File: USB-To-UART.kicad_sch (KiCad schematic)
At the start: 11 parts, among them U2 UMH3N, U4 CH340X

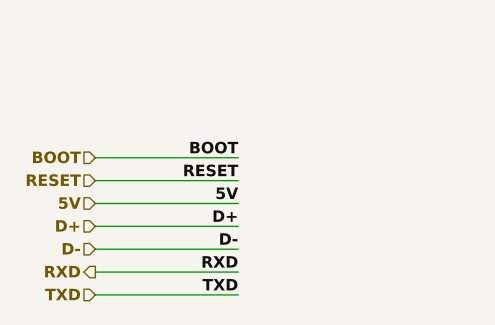
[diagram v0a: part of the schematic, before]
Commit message: Corrected RS485 schematic
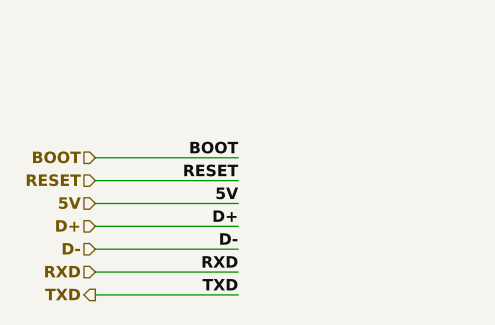
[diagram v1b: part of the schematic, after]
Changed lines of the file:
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@@
     (effects (font (size 1.27 1.27) (thickness 0.254) bold (color 255 0 0 1)) (justify right))
   )
-  (hierarchical_label "TXD" (shape input) (at 31.115 175.895 180) (fields_autoplaced)
+  (hierarchical_label "TXD" (shape output) (at 31.115 175.895 180) (fields_autoplaced)
     (effects (font (size 1.27 1.27) (thickness 0.254) bold (color 0 0 255 1)) (justify right))
   )
@@
     (effects (font (size 1.27 1.27) bold (color 0 194 0 1)) (justify right))
   )
-  (hierarchical_label "RXD" (shape output) (at 31.115 173.355 180) (fields_autoplaced)
+  (hierarchical_label "RXD" (shape input) (at 31.115 173.355 180) (fields_autoplaced)
     (effects (font (size 1.27 1.27) (thickness 0.254) bold (color 0 0 255 1)) (justify right))
   )

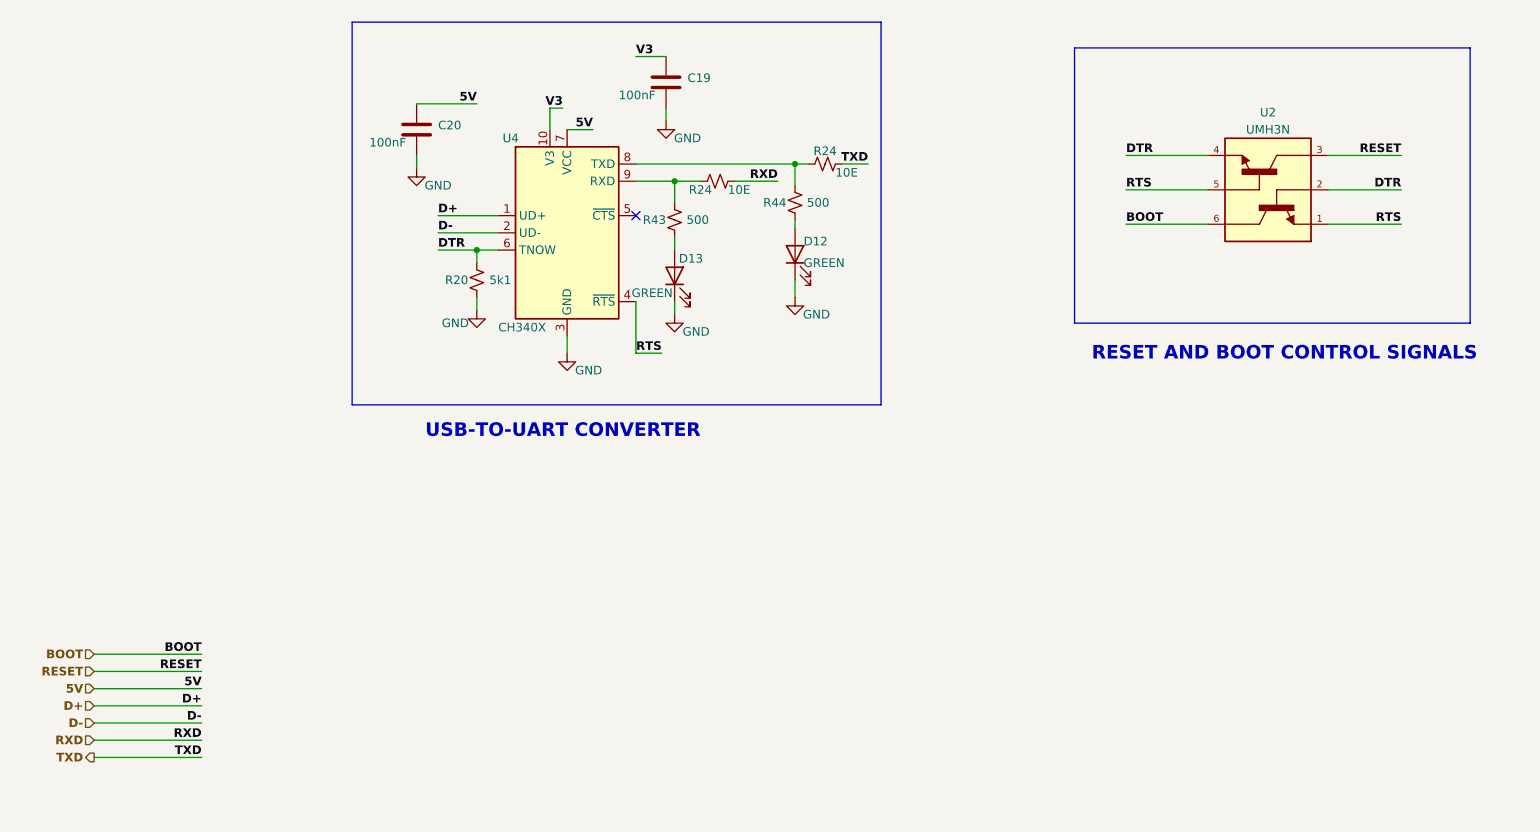
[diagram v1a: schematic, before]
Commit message: Arranged IP5306, Added support for USB-To-RS485
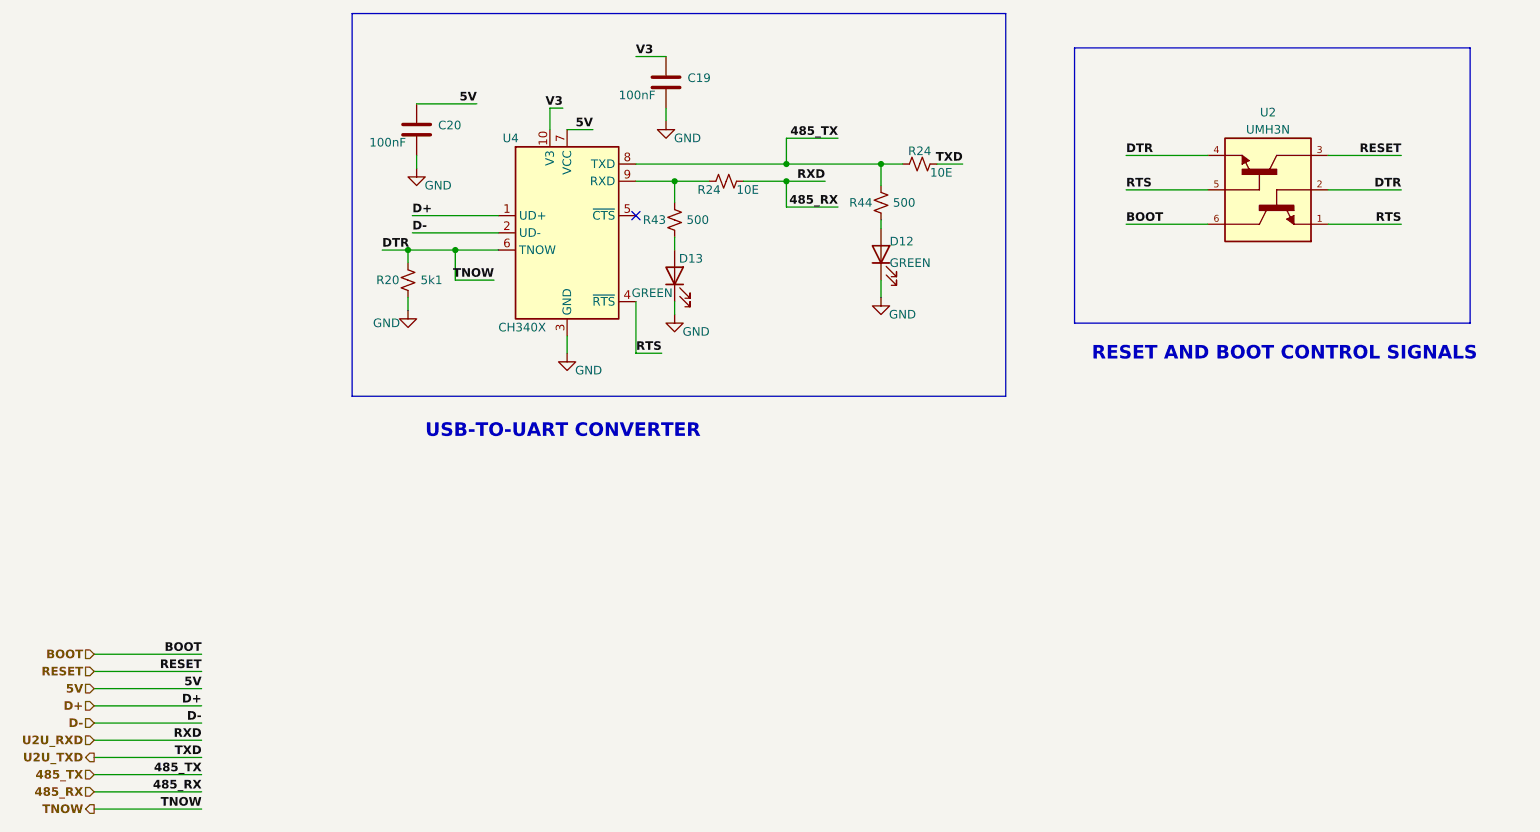
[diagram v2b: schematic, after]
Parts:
- U2: footprint UMH3N:UMT6 -> ESP32-S3_Dev_Board:SC-70-6_L2.2-W1.3-P0.65-LS2.1-BR; Availability In Stock -> (none); Check_prices https://www.snapeda.com/parts/UMH3N/Rohm/view-part/?ref=eda -> (none); MF Rohm -> (none); MP UMH3N -> (none); PN (none) -> UMH3N; Package SOT-363 Rohm -> (none); Price None -> (none); SnapEDA_Link https://www.snapeda.com/parts/UMH3N/Rohm/view-part/?ref=snap -> (none)
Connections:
- net 485_TX: now reaches R24.1, R44.2, U4.8 (TXD)
- net DTR renamed TNOW
- net RXD renamed 485_RX
- net TXD renamed U2U_TXD
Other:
- moved on the sheet: D12, R20, R24, R44

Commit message: Added selection jumper sheet and USB-UART option for board
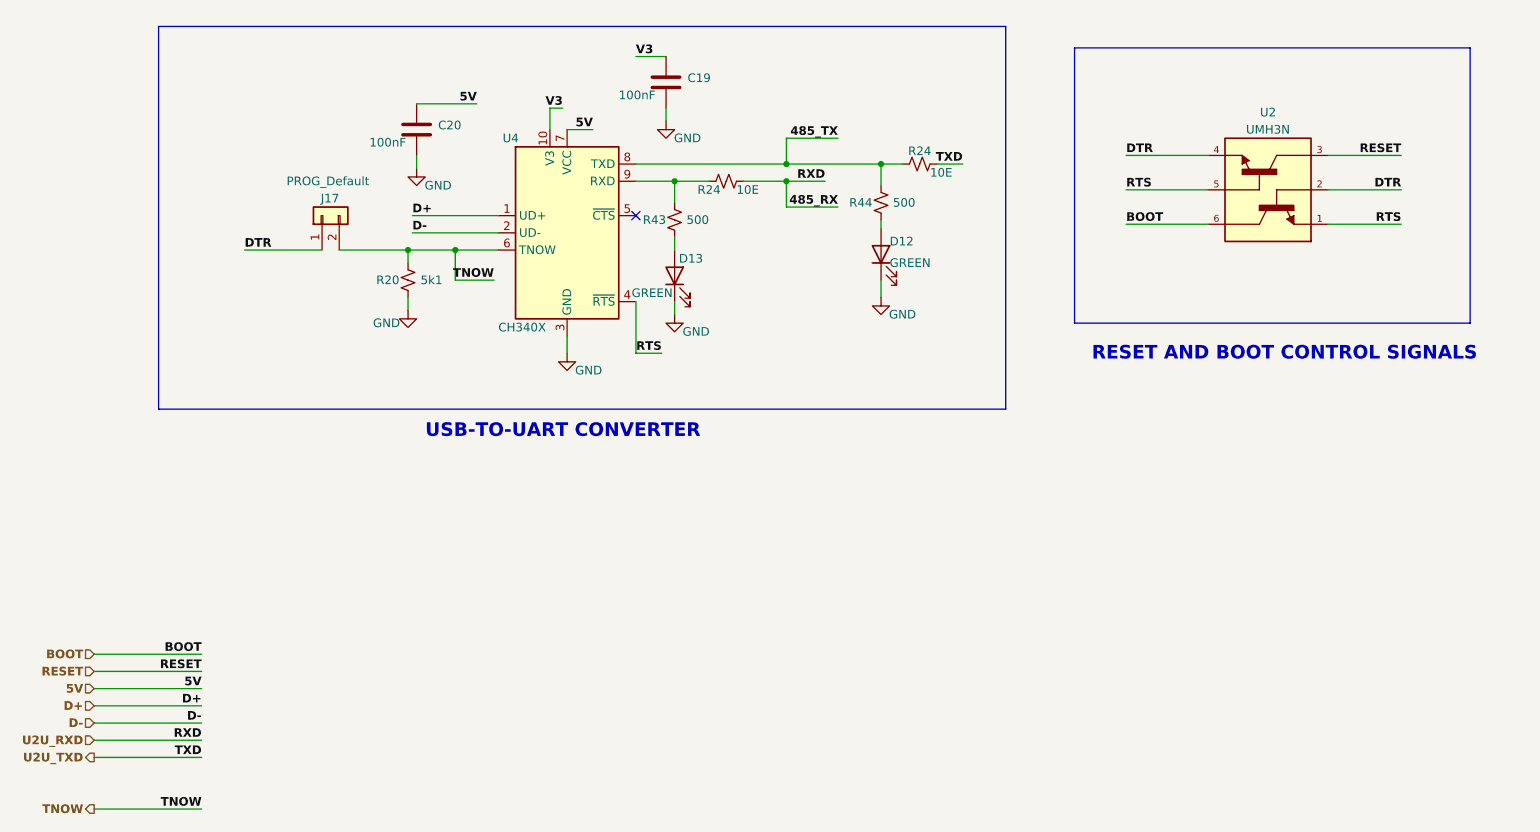
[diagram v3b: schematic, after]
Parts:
- added J17: PROG_Default, ESP32-S3_Dev_Board:PinHeader_1x02_P1.27mm_Vertical, symbol ESP32-S3_DB:Conn_01x02
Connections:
- net TNOW: now also J17.2 (Pin_2); no longer U2.2, U2.4
- net 485_RX renamed U2U_RXD
- new net DTR: J17.1 (Pin_1), U2.2, U2.4
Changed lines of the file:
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@@
   (junction (at 147.32 88.265) (diameter 0) (color 0 0 0 0)
   )
+  (junction (at 133.35 88.265) (diameter 0) (color 0 0 0 0)
+  )
+  (junction (at 116.84 90.805) (diameter 0) (color 0 0 0 0)
+  )
   (junction (at 77.47 100.965) (diameter 0) (color 0 0 0 0)
-  )
-  (junction (at 133.35 88.265) (diameter 0) (color 0 0 0 0)
-  )
-  (junction (at 116.84 90.805) (diameter 0) (color 0 0 0 0)
   )
   (junction (at 84.455 100.965) (diameter 0) (color 0 0 0 0)
@@
     (stroke (width 0) (type default))
   )
+  (wire (pts (xy 77.47 100.965) (xy 77.47 102.87))
+    (stroke (width 0) (type default))
+  )
   (wire (pts (xy 116.84 100.965) (xy 116.84 99.06))
     (stroke (width 0) (type default))
@@
     (stroke (width 0) (type default))
   )
+  (wire (pts (xy 67.31 100.965) (xy 77.47 100.965))
+    (stroke (width 0) (type default))
+  )
   (wire (pts (xy 183.515 97.155) (xy 195.58 97.155))
     (stroke (width 0) (type default))
@@
     (stroke (width 0) (type default))
   )
-  (wire (pts (xy 46.99 178.435) (xy 31.115 178.435))
-    (stroke (width 0.5) (type default) (color 0 0 255 1))
-  )
-  (wire (pts (xy 73.66 100.965) (xy 77.47 100.965))
-    (stroke (width 0) (type default))
-  )
-  (wire (pts (xy 77.47 100.965) (xy 77.47 102.87))
+  (wire (pts (xy 53.34 100.965) (xy 64.77 100.965))
     (stroke (width 0) (type default))
   )
@@
     (stroke (width 0.5) (type default) (color 128 77 0 1))
   )
-  (wire (pts (xy 46.99 180.975) (xy 31.115 180.975))
-    (stroke (width 0.5) (type default) (color 0 0 255 1))
-  )
   (wire (pts (xy 84.455 105.41) (xy 84.455 100.965))
     (stroke (width 0) (type default))
@@
     (stroke (width 1) (type default) (color 72 72 72 1))
   )
-  (bus (pts (xy 165.735 66.04) (xy 165.735 122.555))
+  (bus (pts (xy 165.735 67.945) (xy 165.735 124.46))
     (stroke (width 1) (type default) (color 72 72 72 1))
   )
@@
     (stroke (width 0.5) (type default) (color 0 0 255 1))
   )
-  (bus (pts (xy 69.215 66.04) (xy 165.735 66.04))
+  (bus (pts (xy 40.64 67.945) (xy 165.735 67.945))
     (stroke (width 1) (type default) (color 72 72 72 1))
   )
@@
     (stroke (width 1) (type default) (color 72 72 72 1))
   )
-  (bus (pts (xy 165.735 122.555) (xy 69.215 122.555))
+  (bus (pts (xy 165.735 124.46) (xy 40.64 124.46))
     (stroke (width 1) (type default) (color 72 72 72 1))
   )
@@
     (stroke (width 0) (type default))
   )
-  (bus (pts (xy 69.215 66.04) (xy 69.215 122.555))
+  (bus (pts (xy 40.64 67.945) (xy 40.64 124.46))
     (stroke (width 1) (type default) (color 72 72 72 1))
   )
@@
     (effects (font (size 1.27 1.27) bold (color 132 0 0 1)) (justify right bottom))
   )
-  (label "DTR" (at 73.66 100.965 0) (fields_autoplaced)
+  (label "DTR" (at 53.34 100.965 0) (fields_autoplaced)
     (effects (font (size 1.27 1.27) bold (color 221 133 0 1)) (justify left bottom))
   )
@@
     (effects (font (size 1.27 1.27) bold (color 0 194 0 1)) (justify right bottom))
   )
-  (label "485_TX" (at 46.99 178.435 180) (fields_autoplaced)
-    (effects (font (size 1.27 1.27) bold (color 0 0 255 1)) (justify right bottom))
-  )
   (label "D-" (at 46.99 170.815 180) (fields_autoplaced)
     (effects (font (size 1.27 1.27) bold (color 0 0 255 1)) (justify right bottom))
@@
     (effects (font (size 1.27 1.27) bold (color 0 0 255 1)) (justify right bottom))
   )
-  (label "485_RX" (at 46.99 180.975 180) (fields_autoplaced)
-    (effects (font (size 1.27 1.27) bold (color 0 0 255 1)) (justify right bottom))
-  )
   (label "RTS" (at 224.155 97.155 180) (fields_autoplaced)
     (effects (font (size 1.27 1.27) bold (color 221 133 0 1)) (justify right bottom))
@@
   (label "DTR" (at 183.515 86.995 0) (fields_autoplaced)
     (effects (font (size 1.27 1.27) bold (color 221 133 0 1)) (justify left bottom))
-  )
-  (hierarchical_label "485_RX" (shape input) (at 31.115 180.975 180) (fields_autoplaced)
-    (effects (font (size 1.27 1.27) (thickness 0.254) bold (color 0 0 255 1)) (justify right))
-  )
-  (hierarchical_label "485_TX" (shape input) (at 31.115 178.435 180) (fields_autoplaced)
-    (effects (font (size 1.27 1.27) (thickness 0.254) bold (color 0 0 255 1)) (justify right))
   )
   (hierarchical_label "D-" (shape input) (at 31.115 170.815 180) (fields_autoplaced)
@@
         )
       )
+    )
+  )
+  (symbol (lib_id "ESP32-S3_DB:Conn_01x02") (at 64.77 95.885 90) (unit 1)
+    (in_bom yes) (on_board yes) (dnp no)
+    (property "Reference" "J17" (at 67.31 93.345 90)
+      (effects (font (size 1.27 1.27)) (justify left))
+    )
+    (property "Value" "PROG_Default" (at 71.755 90.805 90)
+      (effects (font (size 1.27 1.27)) (justify left))
+    )
+    (property "Footprint" "ESP32-S3_Dev_Board:PinHeader_1x02_P1.27mm_Vertical" (at 64.77 95.885 0)
+      (effects (font (size 1.27 1.27)) hide)
+    )
+    (property "Datasheet" "~" (at 64.77 95.885 0)
+      (effects (font (size 1.27 1.27)) hide)
+    )
+    (property "PN" "" (at 64.77 95.885 0)
+      (effects (font (size 1.27 1.27)) hide)
+    )
+    (pin "1")
+    (pin "2")
+    (instances
+      (project "ESP32-S3_DB"
+        (path "/b7fc4bd3-c219-4455-832b-8d795385dcf1/e2721808-ce0b-4b73-8382-0fd911e1c931"
+          (reference "J17") (unit 1)
+        )
+        (path "/b7fc4bd3-c219-4455-832b-8d795385dcf1/f98b3539-fa8a-48eb-9a00-f8d7da317cf1"
+          (reference "J20") (unit 1)
+        )
+        (path "/b7fc4bd3-c219-4455-832b-8d795385dcf1/bf189a9b-22e7-430e-8144-dc6e013a917d"
+          (reference "J22") (unit 1)
+        )
+      )

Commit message: Added HW-Tinkerers logo and supporting graphics
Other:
- company: (none) -> HW-TINKERERS (hw.tinkerers@gmail.com)
- title: (none) -> HARDWARE TINKERERS ESP32-S3 DB
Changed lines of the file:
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@@
 (kicad_sch (version 20230121) (generator eeschema)
   (paper "A4")
+  (title_block
+    (title "HARDWARE TINKERERS ESP32-S3 DB")
+    (rev "1.0.0")
+    (company "HW-TINKERERS (hw.tinkerers@gmail.com)")
+    (comment 1 "Email: bhandarkasrishtikr111@gmail.com")
+    (comment 2 "Author: Srishtik Bhandarkar")
+    (comment 3 "Email: vaibhavkhatri00@gmail.com")
+    (comment 4 "Author: Vaibhav Khatri")
+    (comment 5 "Official HW-Tinkerers email: hw.tinkerers@gmail.com")
+  )
   (junction (at 147.32 88.265) (diameter 0) (color 0 0 0 0)
   )

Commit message: Added production files for JLC (BOM and CPL)
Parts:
- C19, C20: LCSC Part Number (none) -> C2173920
- D12, D13: LCSC Part Number (none) -> C84264
- R20: LCSC Part Number (none) -> C105872
- R24: LCSC Part Number (none) -> C102753
- R43, R44: LCSC Part Number (none) -> C137970
- U2: LCSC Part Number (none) -> C62892
- U4: LCSC Part Number (none) -> C3035748
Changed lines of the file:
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@@
+      (effects (font (size 1.27 1.27)) hide)
+    )
+    (property "LCSC Part Number" "C84264" (at 116.84 104.775 0)
       (effects (font (size 1.27 1.27)) hide)
     )
@@
       (effects (font (size 1.27 1.27)) hide)
     )
+    (property "LCSC Part Number" "C137970" (at 147.32 93.98 0)
+      (effects (font (size 1.27 1.27)) hide)
+    )
     (pin "1")
     (pin "2")
@@
       (effects (font (size 1.27 1.27)) hide)
     )
+    (property "LCSC Part Number" "C105872" (at 77.47 105.41 0)
+      (effects (font (size 1.27 1.27)) hide)
+    )
     (pin "1")
     (pin "2")
@@
     )
     (property "PN" "RTT02100JTH" (at 153.035 88.265 0)
+      (effects (font (size 1.27 1.27)) hide)
+    )
+    (property "LCSC Part Number" "C102753" (at 153.035 88.265 0)
       (effects (font (size 1.27 1.27)) hide)
     )
@@
     )
     (property "PN" "RC0402FR-07499RL" (at 116.84 96.52 0)
+      (effects (font (size 1.27 1.27)) hide)
+    )
+    (property "LCSC Part Number" "C137970" (at 116.84 96.52 0)
       (effects (font (size 1.27 1.27)) hide)
     )
@@
     )
     (property "PN" "UMH3N" (at 203.2 86.995 90)
+      (effects (font (size 1.27 1.27)) hide)
+    )
+    (property "LCSC Part Number" "C62892" (at 203.2 86.995 0)
       (effects (font (size 1.27 1.27)) hide)
     )
@@
       (effects (font (size 1.27 1.27)) hide)
     )
+    (property "LCSC Part Number" "C2173920" (at 115.57 76.2 0)
+      (effects (font (size 1.27 1.27)) hide)
+    )
     (pin "1")
     (pin "2")
@@
     )
     (property "PN" "RTT02100JTH" (at 124.46 90.805 0)
+      (effects (font (size 1.27 1.27)) hide)
+    )
+    (property "LCSC Part Number" "C102753" (at 124.46 90.805 0)
       (effects (font (size 1.27 1.27)) hide)
     )
@@
       (effects (font (size 1.27 1.27)) hide)
     )
+    (property "LCSC Part Number" "C2173920" (at 78.74 83.185 0)
+      (effects (font (size 1.27 1.27)) hide)
+    )
     (pin "1")
     (pin "2")
@@
     )
     (property "PN" "NCD0603C1" (at 147.32 101.6 0)
+      (effects (font (size 1.27 1.27)) hide)
+    )
+    (property "LCSC Part Number" "C84264" (at 147.32 101.6 0)
       (effects (font (size 1.27 1.27)) hide)
     )
@@
       (effects (font (size 1.27 1.27)) hide)
     )
+    (property "LCSC Part Number" "C3035748" (at 100.965 98.425 0)
+      (effects (font (size 1.27 1.27)) hide)
+    )
